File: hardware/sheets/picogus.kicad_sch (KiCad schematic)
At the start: 58 parts, among them J1 DMA_JP, J5 SWD, SW1 BOOTSEL, U1 RP2040, U10 74LVC2G06, U11 APS6404L, U12 PCM5102A, U2 W25Q128JVS, U3 AMS1117-3.3, U4 CB3T3257, U5 CB3T3257, U7 74AHC14, U8 74LVC00, U9 74LVC00, Y1 12MHz

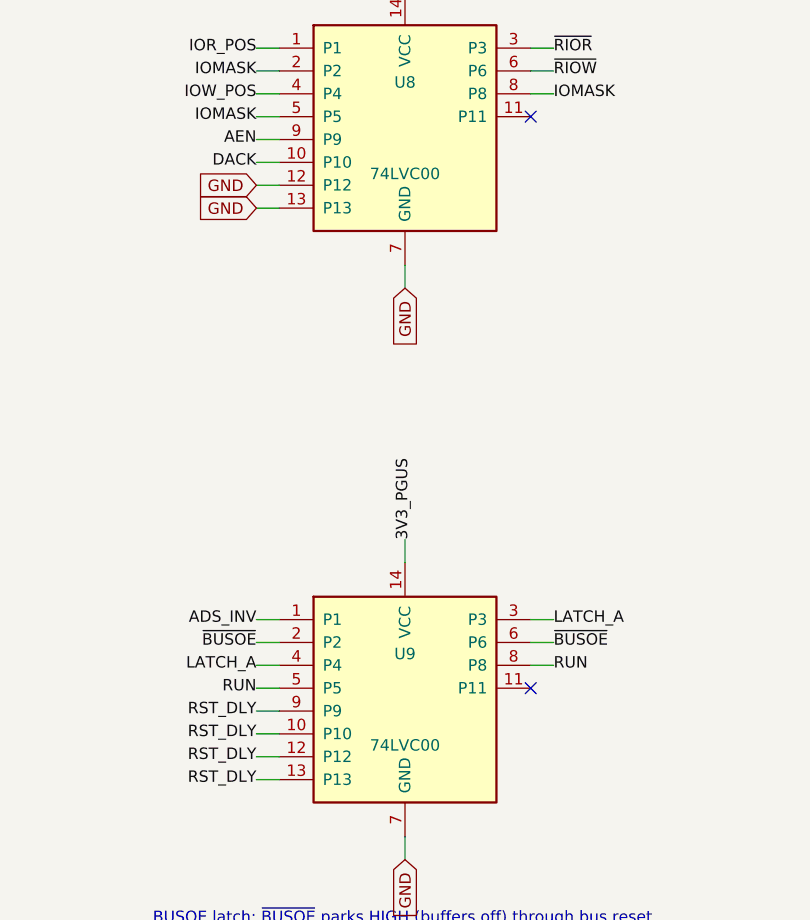
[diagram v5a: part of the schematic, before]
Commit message: picogus: U8/U9 74LVC00 -> 74HC00 (basic part; LVC was a 5V-reference fossil)
The LVC grade came from polpo's 5V-ISA reference design; this island has
been all-3.3V since the redesign, so every input is 3.3V-driven and plain
HC is in spec. 74HC00 (C699445) is a basic-library line already shared
with parallel/addr_decode; the orphaned 74LVC00 parts.py entry -- the
board's thinnest BOM line (~125 units) -- is deleted.

Co-Authored-By: Claude Fable 5 <noreply@anthropic.com>
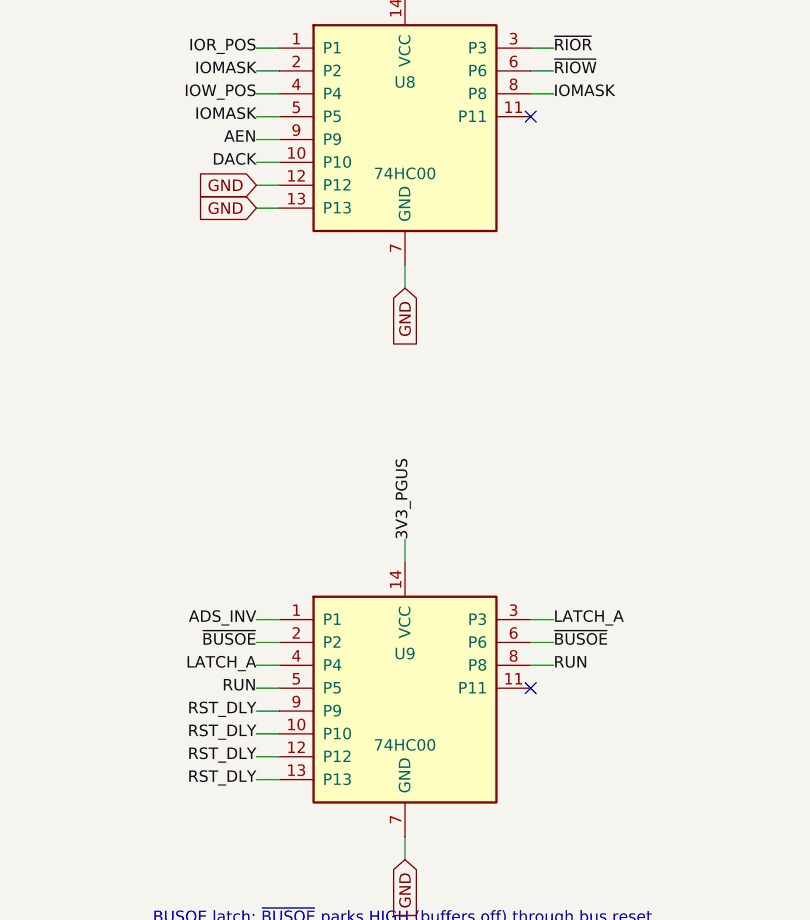
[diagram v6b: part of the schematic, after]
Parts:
- U8, U9: value 74LVC00 -> 74HC00; LCSC Part Num C526338 -> C699445
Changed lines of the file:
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@@
 			)
 		)
-		(property "Value" "74LVC00"
+		(property "Value" "74HC00"
 			(at 355.6 132.08 0)
 			(effects
@@
 			)
 		)
-		(property "LCSC Part Num" "C526338"
+		(property "LCSC Part Num" "C699445"
 			(at 355.6 127 0)
 			(effects
@@
 			)
 		)
-		(property "Value" "74LVC00"
+		(property "Value" "74HC00"
 			(at 355.6 195.58 0)
 			(effects
@@
 			)
 		)
-		(property "LCSC Part Num" "C526338"
+		(property "LCSC Part Num" "C699445"
 			(at 355.6 190.5 0)
 			(effects

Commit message: Passives: basic-library audit + 4x resistor-array pull consolidation
Audit: every discrete R/C value was already JLC basic except the ferrite
beads -- swapped to basic Murata BLM18PG121SN1D (C14709, 120R@100MHz,
same family/role). The 100uF electrolytic and buck inductor stay
extended (zero fee-free parts exist in those subcategories). Pruned the
orphaned 5V-era 47nF/330nF MAX3241 cap entries.

Pull consolidation: 65 discrete 10k/4.7k rail pulls across 8 sheets
collapse into 18 basic 4-element isolated arrays (4D03WGJ0103T5E /
4D03WGJ0472T5E, element k = pins k/9-k; new mxbus.r_pack4 helper).
Isolated elements let packs mix rails; every net keeps its exact rail
and semantics (verified element-by-element in the netlist). RC/divider/
series/I2C resistors stay discrete. Board 452 -> 406 components; also
de-risks the sole basic 10k 0603 line (0 stock at audit). Audit
recorded in jlcpcb-sourcing.md.

Co-Authored-By: Claude Fable 5 <noreply@anthropic.com>
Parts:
- FB1, FB2: value 100R@100MHz -> 120R@100MHz; LCSC Part Num C160981 -> C14709
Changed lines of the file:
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@@
 			)
 		)
-		(property "Value" "100R@100MHz"
+		(property "Value" "120R@100MHz"
 			(at 50.8 93.98 0)
 			(effects
@@
 			)
 		)
-		(property "LCSC Part Num" "C160981"
+		(property "LCSC Part Num" "C14709"
 			(at 50.8 88.9 0)
 			(effects
@@
 			)
 		)
-		(property "Value" "100R@100MHz"
+		(property "Value" "120R@100MHz"
 			(at 50.8 106.68 0)
 			(effects
@@
 			)
 		)
-		(property "LCSC Part Num" "C160981"
+		(property "LCSC Part Num" "C14709"
 			(at 50.8 101.6 0)
 			(effects
